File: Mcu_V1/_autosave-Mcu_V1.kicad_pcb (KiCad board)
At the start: 2 copper layers, 47.8 x 31.5 mm, 29 parts, among them J1 Conn_01x04_Pin, J2 Conn_01x09_Pin, J3 Conn_01x04_Pin, J4 Conn_02x03_Odd_Even, U1 24LC1025, U2 DS1337S_, U3 24LC1025, U4 ATMEGA328P-AU, Y1 32.768 KHz, Y2 16MHz

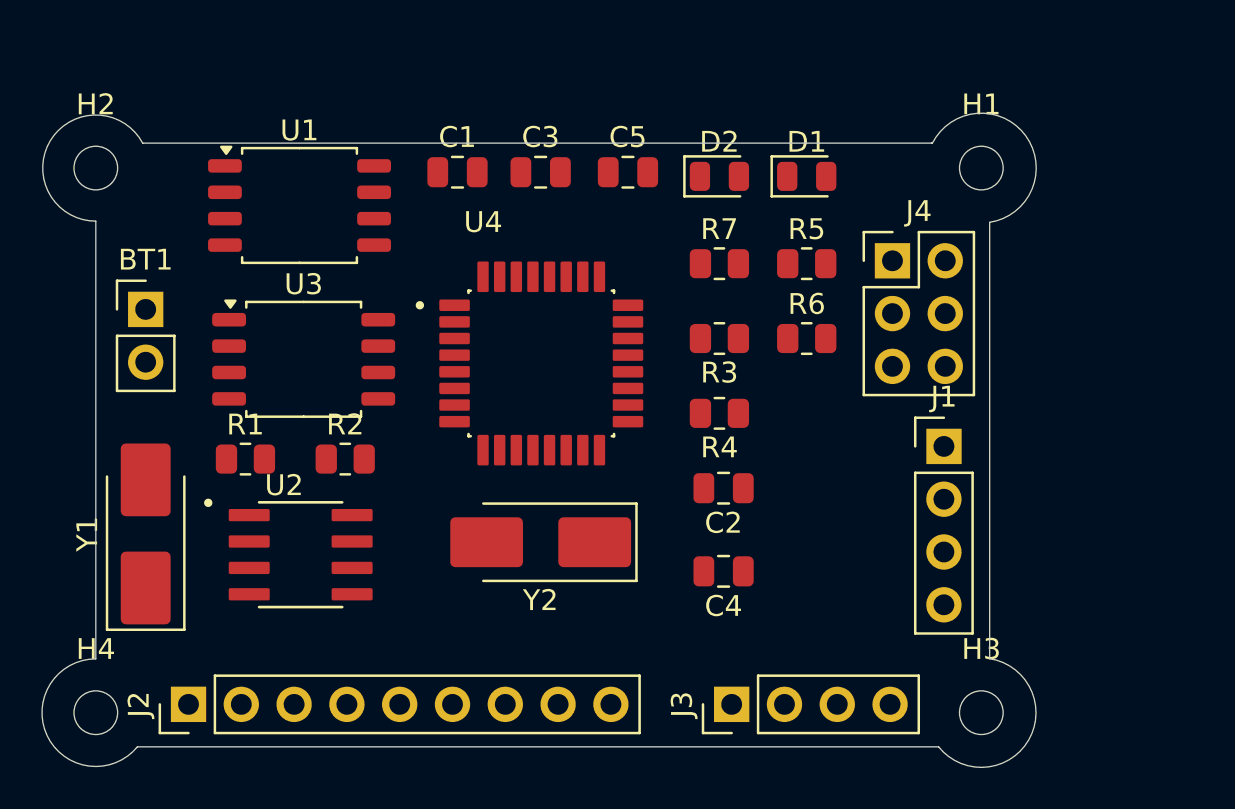
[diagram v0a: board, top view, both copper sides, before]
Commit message: traces done
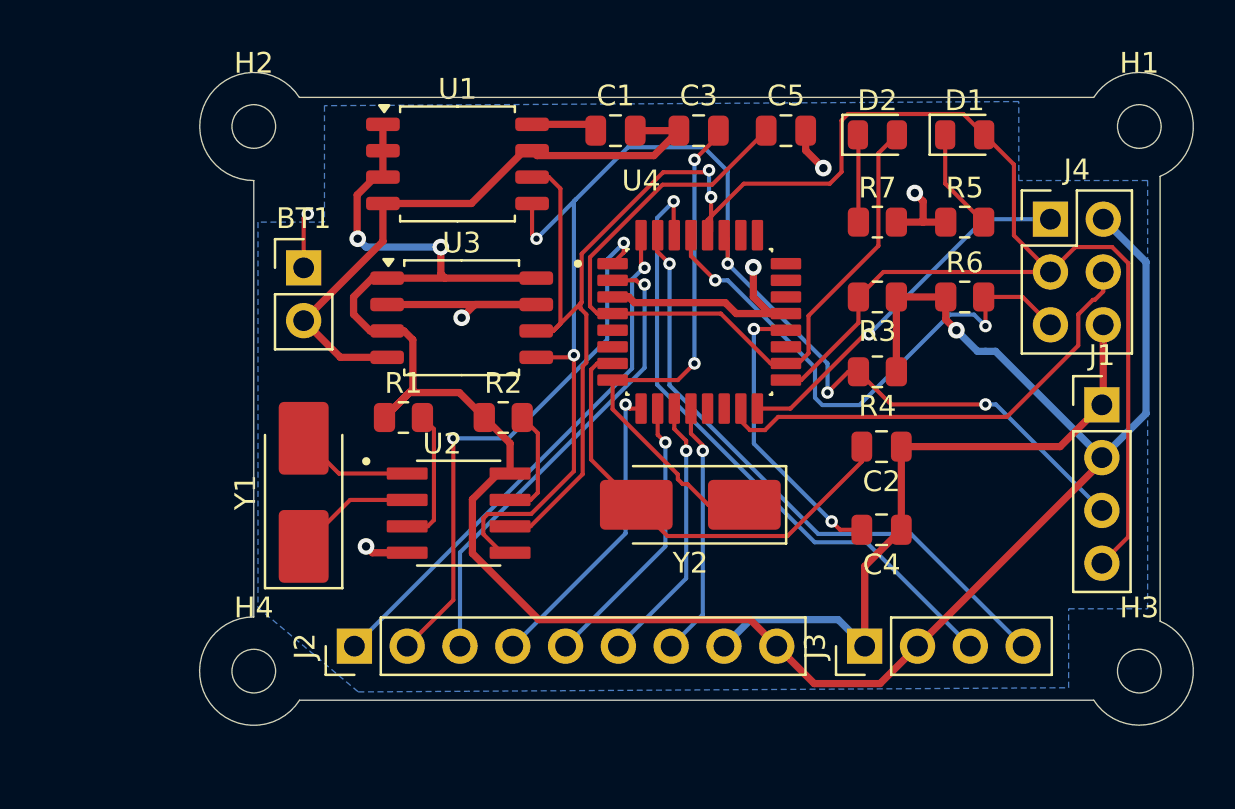
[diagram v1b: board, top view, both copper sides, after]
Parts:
- moved J2 8.46 mm to (144.8, 105.0)
- moved J1 7.86 mm to (180.8, 93.4)
- moved U1 7.86 mm to (149.8, 81.8)
- moved BT1 7.86 mm to (142.4, 86.8)
- moved C1 7.86 mm to (157.4, 80.2)
- moved C2 7.86 mm to (170.2, 95.4)
- moved C3 7.86 mm to (161.4, 80.2)
- moved C4 7.86 mm to (170.2, 99.4)
- moved C5 7.86 mm to (165.6, 80.2)
- moved D1 7.86 mm to (174.2, 80.4)
- moved D2 7.86 mm to (170.0, 80.4)
- moved H1 7.86 mm to (182.6, 80.0)
- moved H2 7.86 mm to (140.0, 80.0)
- moved H3 7.86 mm to (182.6, 106.2)
- moved H4 7.86 mm to (140.0, 106.2)
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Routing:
- net /Vcc: track 0.00 -> 114.8 mm, vias 0 -> 3
- net /SCK: track 0.00 -> 98.7 mm, vias 0 -> 2
- net GND: track 0.00 -> 93.7 mm, vias 0 -> 5
- net /SDA: track 0.00 -> 67.0 mm, vias 0 -> 5
- net Net-(BT1-+): track 0.00 -> 40.2 mm, vias 0 -> 1
- net /RX: track 0.00 -> 31.1 mm, vias 0 -> 1
- net /TX: track 0.00 -> 29.7 mm, vias 0 -> 1
- net /D3: track 0.00 -> 26.5 mm, vias 0 -> 2
- net /RESET: track 0.00 -> 26.2 mm, vias 0 -> 2
- net Net-(U4-PB7): track 0.00 -> 25.7 mm, vias 0 -> 2
- net /D2: track 0.00 -> 25.7 mm, vias 0 -> 1
- net /MOSI: track 0.00 -> 22.8 mm
- net /D4: track 0.00 -> 22.7 mm, vias 0 -> 1
- net Net-(U4-PB6): track 0.00 -> 22.2 mm
- net /MISO: track 0.00 -> 17.9 mm, vias 0 -> 1
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- added copper zone on B.Cu, net GND
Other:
- board size 47.8 x 31.5 mm -> 47.8 x 31.4 mm
